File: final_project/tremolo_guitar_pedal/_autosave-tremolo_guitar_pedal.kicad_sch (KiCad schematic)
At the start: 34 parts, among them CN3 NUCLEO-L432KC, CN4 NUCLEO-L432KC, J1 NJ2FD-V, J2 NJ2FD-V, J3 UPduino v3.1, J5 UPduino v3.1, SW1 3PDT Footswitch, U1 NE5532, U2 PCM5102, U3 LD1117DT33CTR

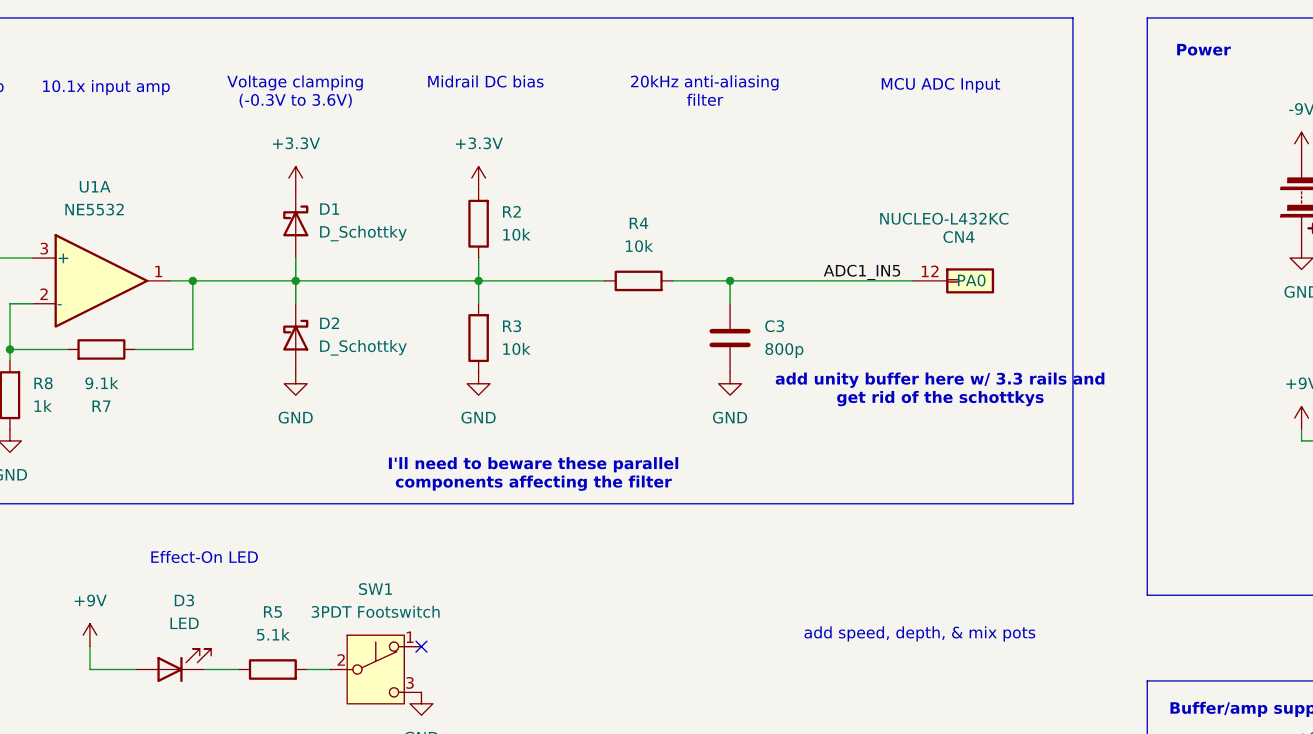
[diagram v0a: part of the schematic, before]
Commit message: Cleaning up code from a couple different labs
For redos
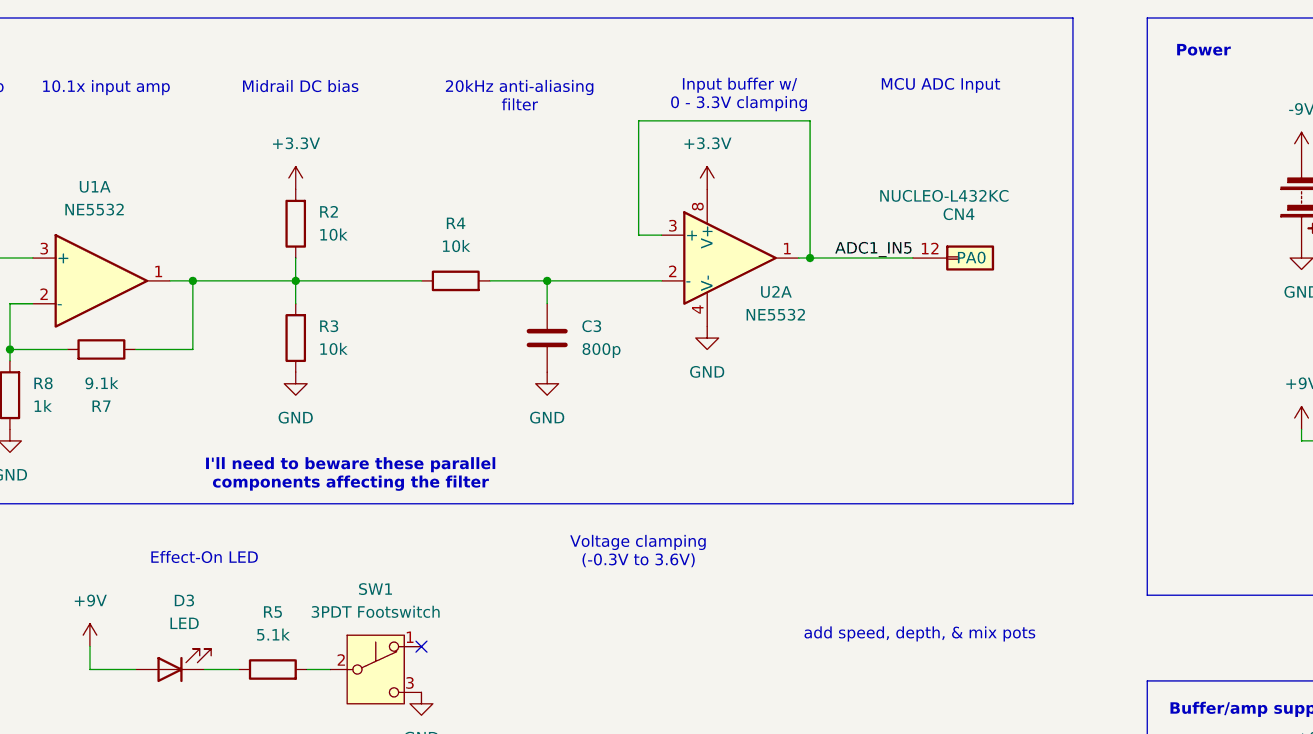
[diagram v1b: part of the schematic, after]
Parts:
- removed D1, D2: D_Schottky, symbol Device:D_Schottky
- added U2, U4: NE5532, symbol Amplifier_Operational:NE5532
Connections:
- net +3.3V: now also U4.8 (V+)
- net ADC1_IN5: now also U2.1, U2.3 (+); no longer C3.1, R4.2
- net GND: now also U4.4 (V-)
- new net: C3.1, R4.2, U2.2 (-)
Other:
- note added: "Input buffer w/ 0 - 3.3V clamping"
- note removed: "add unity buffer here w/ 3.3 rails and get rid of the schottkys"
- moved on the sheet: C3, CN4, R2, R3, R4
